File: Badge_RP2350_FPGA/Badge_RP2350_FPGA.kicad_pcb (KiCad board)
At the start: 2 copper layers, 100 x 150 mm, 102 parts, among them J1 USB_C_Receptacle_USB2.0_16P, J2 Conn_01x03_Pin, J3 Conn_01x15_Pin, J4 Conn_01x15_Pin, SW1 SW_Push, SW12 On/Off, SW2 SW_Push, U1 RP2350_60QFN, U2 GW1N-LV9QN88C6_I5_, U3 ME6211C12, U4 TMI7003C, U6 W25Q32JVSS, U7 W25Q32JVSS, Y1 ABM8-272-T3

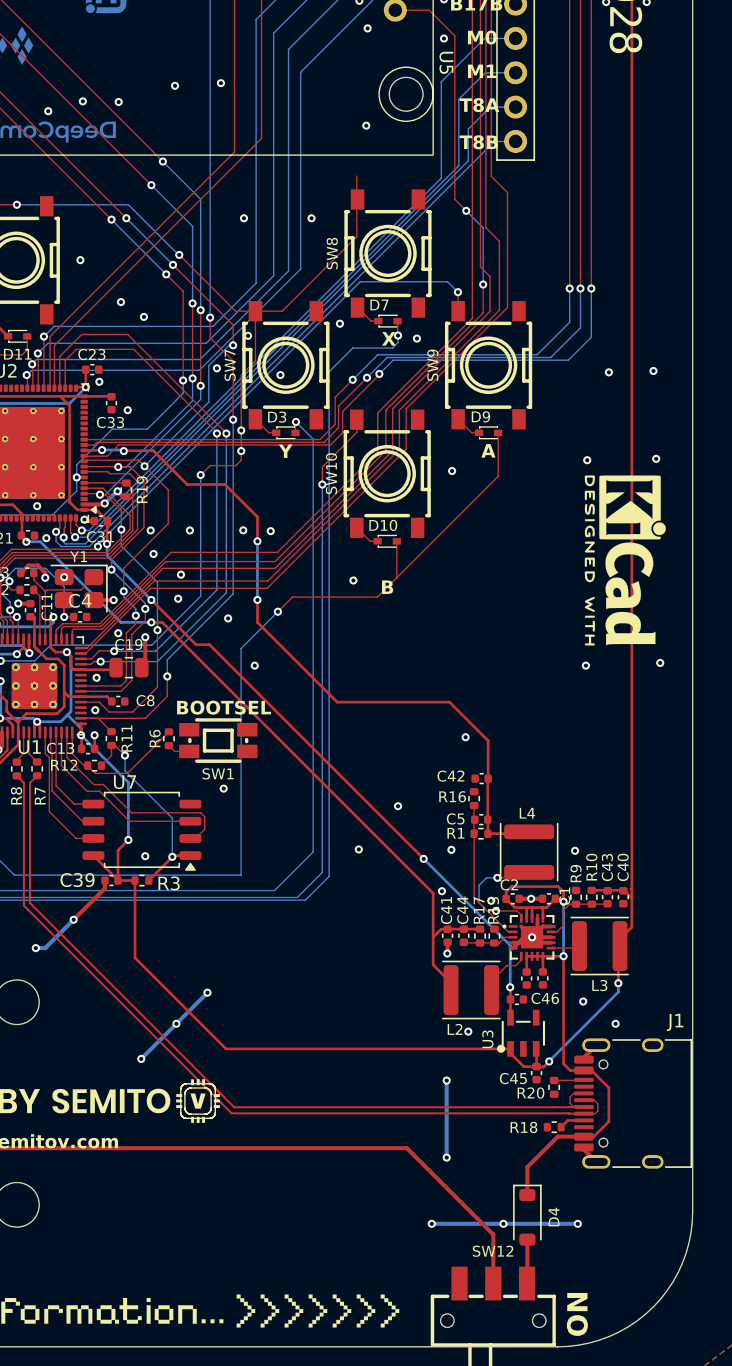
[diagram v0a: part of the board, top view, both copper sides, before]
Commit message: fix power boost issue
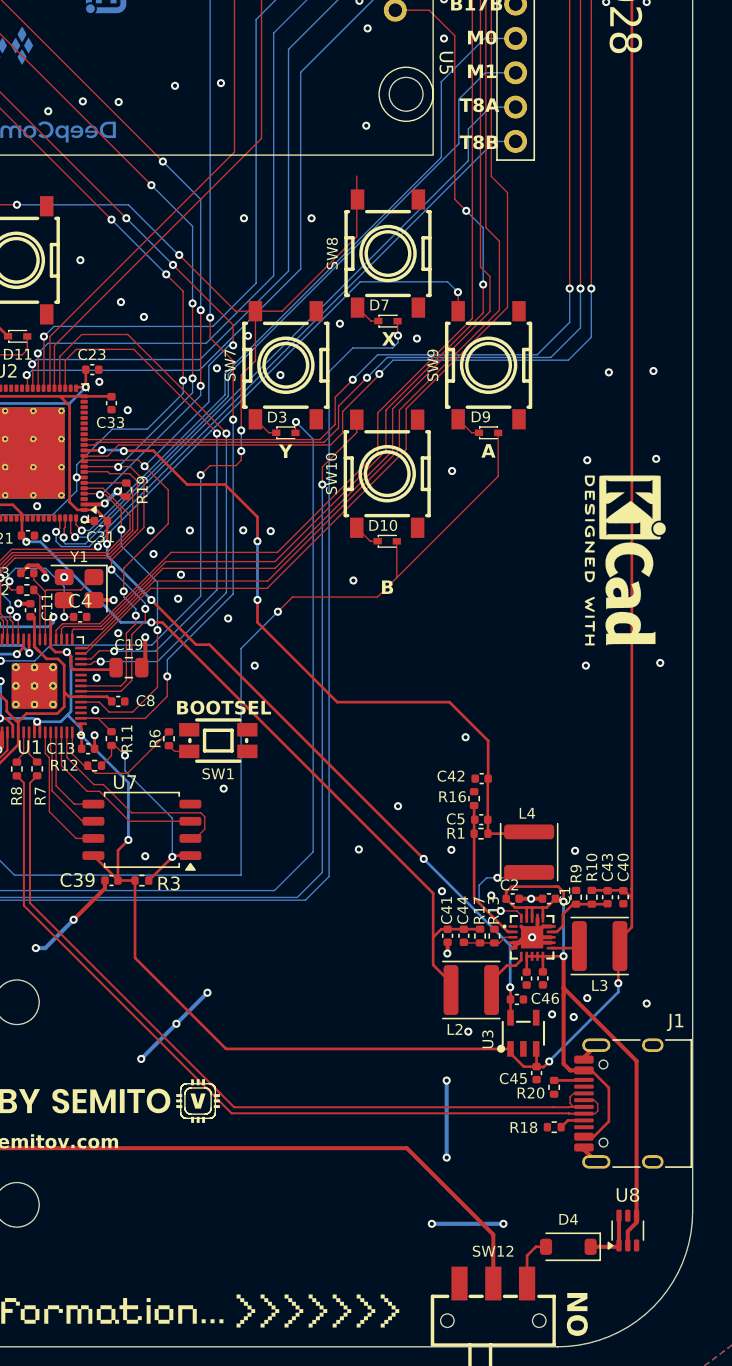
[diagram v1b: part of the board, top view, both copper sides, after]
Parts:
- added U8: TPS61221DCK, Package_TO_SOT_SMD:Texas_R-PDSO-G6, F.Cu at (145.2, 191.4)
- moved D4 3.73 mm to (140.8, 192.6), turned to 180 degrees
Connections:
- D4 pad 1: VBUS -> Net-(D4-K)
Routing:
- net VBUS: track 45.7 -> 60.1 mm
- net GND: track 112.3 -> 106.8 mm, vias 172 -> 173
- net Net-(D4-K): track 0.00 -> 4.34 mm
- net Net-(D4-A): track 3.26 -> 3.76 mm
